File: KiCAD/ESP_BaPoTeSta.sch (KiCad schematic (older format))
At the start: 17 parts, among them P1 Progr, P2 Battery, P3 Power, SW1 Upload, SW2 Reset, U1 MCP1700-3302E, U2 ESP-12, U3 DS18B20

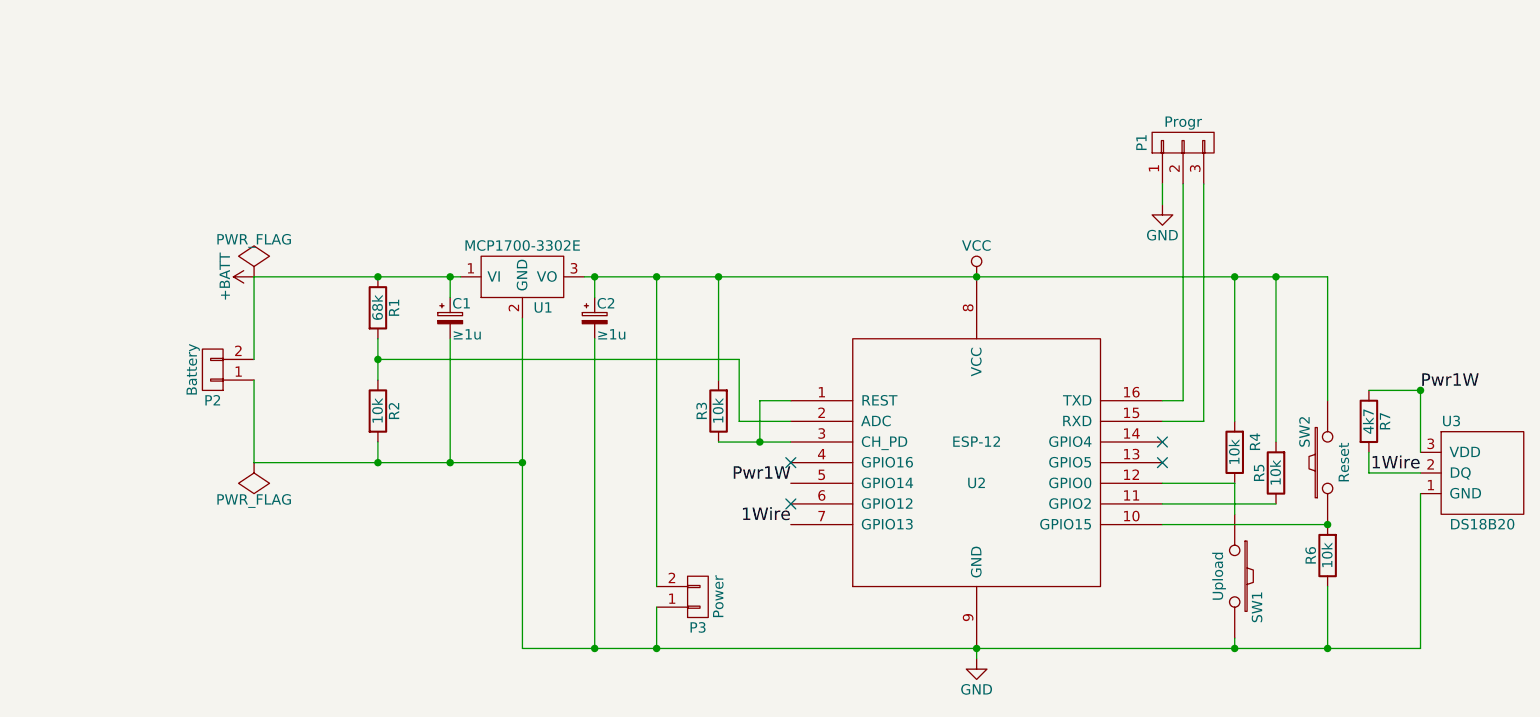
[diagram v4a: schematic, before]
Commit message: WIP: Redesign PCB
Use SMD resistors, and start to work on #14, #15 and #16
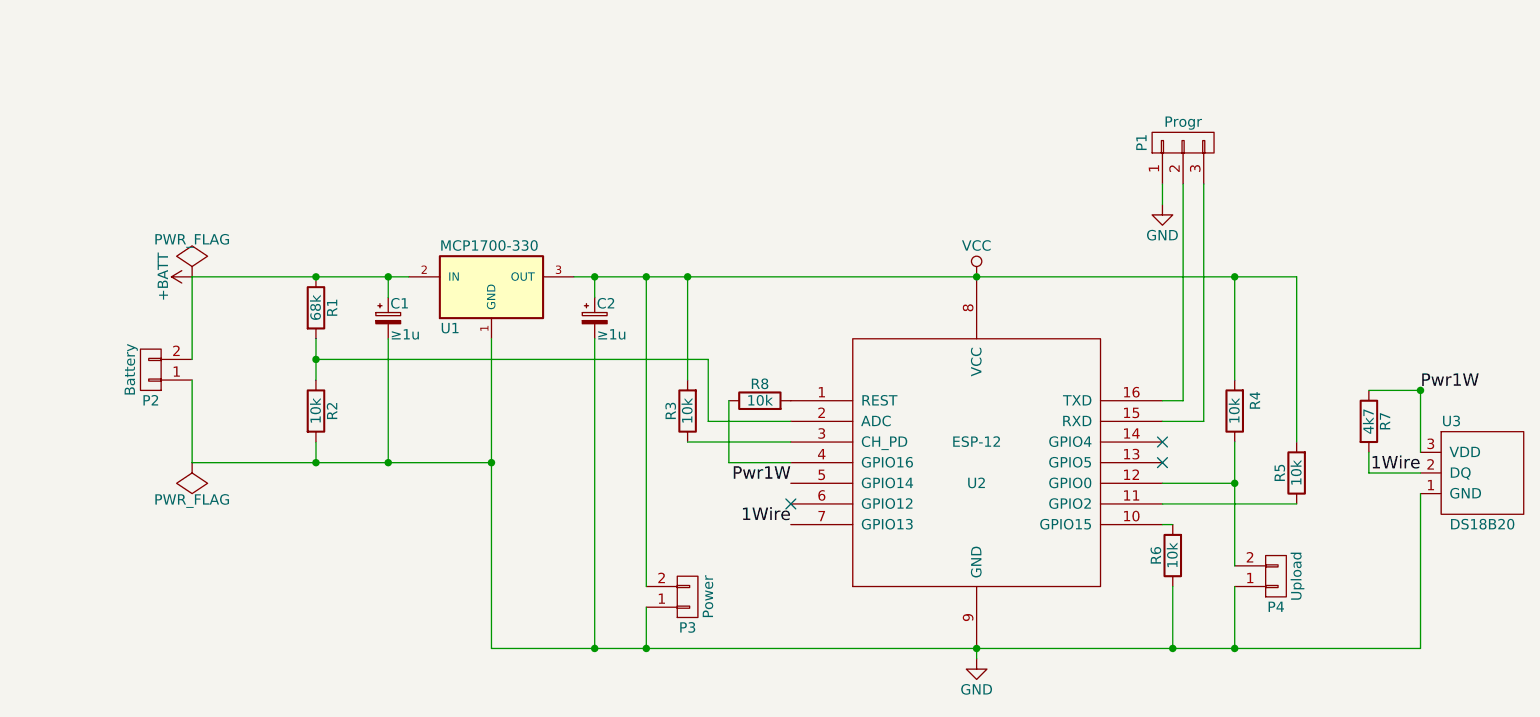
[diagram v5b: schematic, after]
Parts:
- removed SW1: Upload, Buttons_Switches_ThroughHole:SW_PUSH_SMALL, symbol SW_PUSH
- removed SW2: Reset, Buttons_Switches_ThroughHole:SW_PUSH_SMALL, symbol SW_PUSH
- removed U1: MCP1700-3302E, TO_SOT_Packages_THT:TO-92_Inline_Wide, symbol MCP1754ST-3302E/MB
- added P4: Upload, Pin_Headers:Pin_Header_Straight_1x02, symbol CONN_01X02
- added R8: 10k, Resistors_SMD:R_1206_HandSoldering, symbol R
- added U1: MCP1700-330, TO_SOT_Packages_THT:TO-92_Inline_Narrow_Oval, symbol LM7905CT
- R1, R2, R3, R4, R5, R6, R7: footprint Resistors_ThroughHole:Resistor_Horizontal_RM10mm -> Resistors_SMD:R_1206_HandSoldering
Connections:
- net +BATT: now also U1.2 (IN)
- net GND: now also P4.1 (P1), U1.1 (GND)
- net VCC: now also U1.3 (OUT)
- net at R3.1, U2.3 (CH_PD): no longer U2.1 (REST)
- net at R4.1, U2.12 (GPIO0): now also P4.2 (P2)
- net at U2.4 (GPIO16): now also R8.1
- new net: R8.2, U2.1 (REST)
- no-connect marks 4 -> 3
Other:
- moved on the sheet: C1, P2, P3, R1, R2, R3, R4, R5, R6

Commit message: WIP: Continue improving PCB
continue the work started in 0493dcc
add additional header to enter config mode
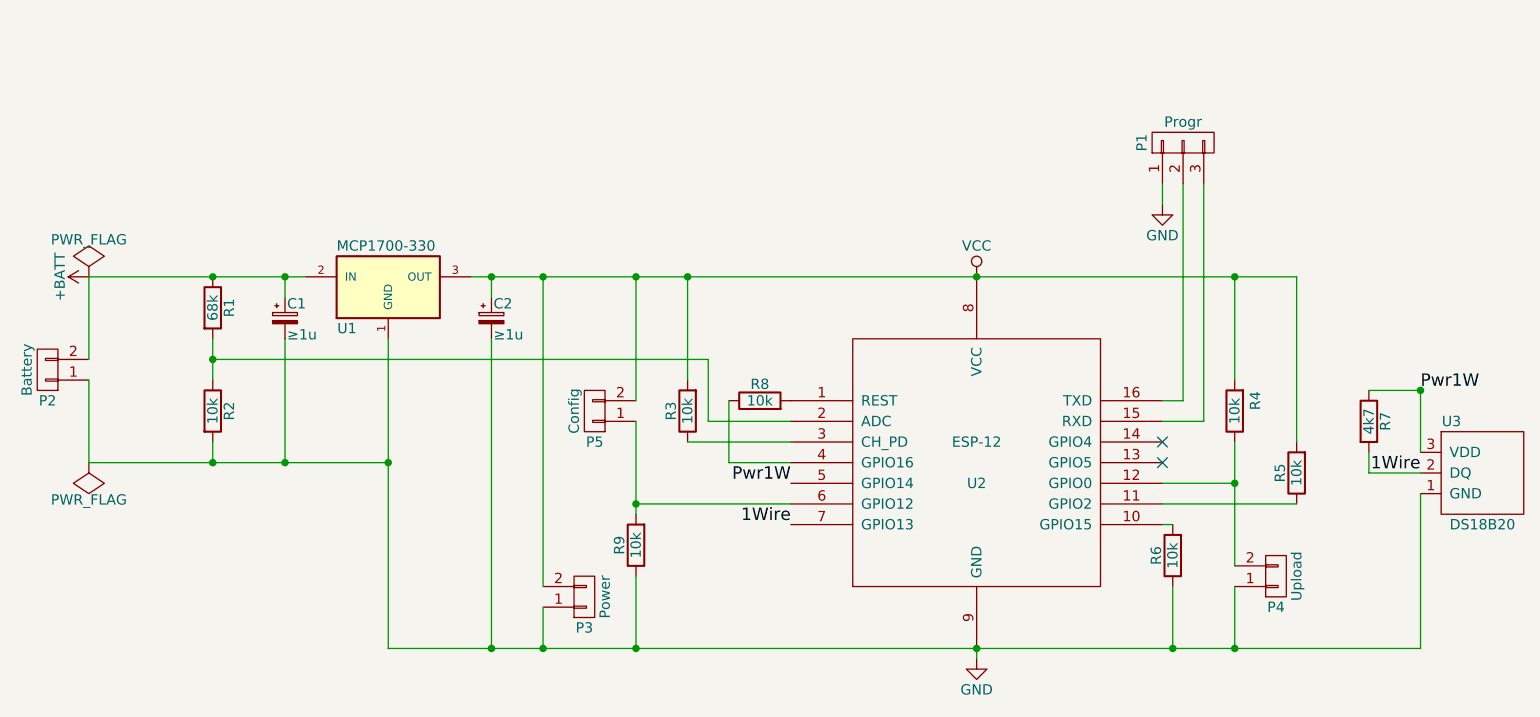
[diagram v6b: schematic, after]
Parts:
- added P5: Config, Pin_Headers:Pin_Header_Straight_1x02, symbol CONN_01X02
- added R9: 10k, Resistors_SMD:R_1206_HandSoldering, symbol R
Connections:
- net GND: now also R9.1
- net VCC: now also P5.2 (P2)
- net at U2.6 (GPIO12): now also P5.1 (P1), R9.2
- no-connect marks 3 -> 2
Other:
- moved on the sheet: C1, C2, P2, P3, R1, R2, U1
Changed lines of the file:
@@
 L R R1
 U 1 1 56629976
-P 2650 2250
-F 0 "R1" V 2730 2250 50  0000 C CNN
-F 1 "68k" V 2650 2250 50  0000 C CNN
-F 2 "Resistors_SMD:R_1206_HandSoldering" V 2580 2250 50  0001 C CNN
-F 3 "" H 2650 2250 50  0000 C CNN
-	1    2650 2250
+P 2150 2250
+F 0 "R1" V 2230 2250 50  0000 C CNN
+F 1 "68k" V 2150 2250 50  0000 C CNN
+F 2 "Resistors_SMD:R_1206_HandSoldering" V 2080 2250 50  0001 C CNN
+F 3 "" H 2150 2250 50  0000 C CNN
+	1    2150 2250
 	1    0    0    -1
 $EndComp
@@
 L R R2
 U 1 1 566299C7
-P 2650 2750
-F 0 "R2" V 2730 2750 50  0000 C CNN
-F 1 "10k" V 2650 2750 50  0000 C CNN
-F 2 "Resistors_SMD:R_1206_HandSoldering" V 2580 2750 50  0001 C CNN
-F 3 "" H 2650 2750 50  0000 C CNN
-	1    2650 2750
+P 2150 2750
+F 0 "R2" V 2230 2750 50  0000 C CNN
+F 1 "10k" V 2150 2750 50  0000 C CNN
+F 2 "Resistors_SMD:R_1206_HandSoldering" V 2080 2750 50  0001 C CNN
+F 3 "" H 2150 2750 50  0000 C CNN
+	1    2150 2750
 	1    0    0    -1
 $EndComp
@@
 Connection ~ 6800 3900
 Wire Wire Line
-	3500 2400 3500 3900
-Wire Wire Line
-	2050 3000 3500 3000
-Wire Wire Line
-	2650 3000 2650 2900
-Wire Wire Line
-	2050 2100 3100 2100
-Wire Wire Line
-	2650 2400 2650 2600
-Connection ~ 2650 2100
-Connection ~ 2650 3000
-Connection ~ 2650 2500
+	3000 2400 3000 3900
+Wire Wire Line
+	1550 3000 3000 3000
+Wire Wire Line
+	2150 3000 2150 2900
+Wire Wire Line
+	1550 2100 2600 2100
+Wire Wire Line
+	2150 2400 2150 2600
+Connection ~ 2150 2100
+Connection ~ 2150 3000
+Connection ~ 2150 2500
 Wire Wire Line
 	4950 2800 4550 2800
@@
 Wire Wire Line
 	8000 3900 8000 3150
-NoConn ~ 4950 3200
 NoConn ~ 6750 2900
 $Comp
@@
 	5850 3900 5850 3950
 Wire Wire Line
-	3500 3900 8000 3900
+	3000 3900 8000 3900
 Connection ~ 4450 2100
 Connection ~ 5850 3900
-Connection ~ 3500 3000
-Wire Wire Line
-	4550 2500 2650 2500
+Connection ~ 3000 3000
+Wire Wire Line
+	4550 2500 2150 2500
 $Comp
 L PWR_FLAG #FLG04
 U 1 1 5662B03F
-P 2050 2100
-F 0 "#FLG04" H 2050 2195 50  0001 C CNN
-F 1 "PWR_FLAG" H 2050 2280 50  0000 C CNN
-F 2 "" H 2050 2100 50  0000 C CNN
-F 3 "" H 2050 2100 50  0000 C CNN
-	1    2050 2100
+P 1550 2100
+F 0 "#FLG04" H 1550 2195 50  0001 C CNN
+F 1 "PWR_FLAG" H 1550 2280 50  0000 C CNN
+F 2 "" H 1550 2100 50  0000 C CNN
+F 3 "" H 1550 2100 50  0000 C CNN
+	1    1550 2100
 	1    0    0    -1
 $EndComp
@@
 L PWR_FLAG #FLG05
 U 1 1 5662B14A
-P 2050 3000
-F 0 "#FLG05" H 2050 3095 50  0001 C CNN
-F 1 "PWR_FLAG" H 2050 3180 50  0000 C CNN
-F 2 "" H 2050 3000 50  0000 C CNN
-F 3 "" H 2050 3000 50  0000 C CNN
-	1    2050 3000
+P 1550 3000
+F 0 "#FLG05" H 1550 3095 50  0001 C CNN
+F 1 "PWR_FLAG" H 1550 3180 50  0000 C CNN
+F 2 "" H 1550 3000 50  0000 C CNN
+F 3 "" H 1550 3000 50  0000 C CNN
+	1    1550 3000
 	-1   0    0    1
 $EndComp
@@
 L CP_Small C1
 U 1 1 5662B5FD
-P 3000 2300
-F 0 "C1" H 3010 2370 50  0000 L CNN
-F 1 "≥1u" H 3010 2220 50  0000 L CNN
-F 2 "Capacitors_ThroughHole:C_Radial_D5_L11_P2" H 3000 2300 50  0001 C CNN
-F 3 "" H 3000 2300 50  0000 C CNN
-	1    3000 2300
+P 2500 2300
+F 0 "C1" H 2510 2370 50  0000 L CNN
+F 1 "≥1u" H 2510 2220 50  0000 L CNN
+F 2 "Capacitors_ThroughHole:C_Radial_D5_L11_P2" H 2500 2300 50  0001 C CNN
+F 3 "" H 2500 2300 50  0000 C CNN
+	1    2500 2300
 	1    0    0    -1
 $EndComp
@@
 L CP_Small C2
 U 1 1 5662B72E
-P 4000 2300
-F 0 "C2" H 4010 2370 50  0000 L CNN
-F 1 "≥1u" H 4010 2220 50  0000 L CNN
-F 2 "Capacitors_ThroughHole:C_Radial_D5_L11_P2" H 4000 2300 50  0001 C CNN
-F 3 "" H 4000 2300 50  0000 C CNN
-	1    4000 2300
-	1    0    0    -1
-$EndComp
-Wire Wire Line
-	4000 2200 4000 2100
-Connection ~ 4000 2100
-Wire Wire Line
-	4000 2400 4000 3900
-Connection ~ 4000 3900
-Wire Wire Line
-	3000 2200 3000 2100
-Connection ~ 3000 2100
-Wire Wire Line
-	3000 2400 3000 3000
-Connection ~ 3000 3000
+P 3500 2300
+F 0 "C2" H 3510 2370 50  0000 L CNN
+F 1 "≥1u" H 3510 2220 50  0000 L CNN
+F 2 "Capacitors_ThroughHole:C_Radial_D5_L11_P2" H 3500 2300 50  0001 C CNN
+F 3 "" H 3500 2300 50  0000 C CNN
+	1    3500 2300
+	1    0    0    -1
+$EndComp
+Wire Wire Line
+	3500 2200 3500 2100
+Connection ~ 3500 2100
+Wire Wire Line
+	3500 2400 3500 3900
+Connection ~ 3500 3900
+Wire Wire Line
+	2500 2200 2500 2100
+Connection ~ 2500 2100
+Wire Wire Line
+	2500 2400 2500 3000
+Connection ~ 2500 3000
 Wire Wire Line
 	7100 2900 7100 3500
@@
 L CONN_01X02 P2
 U 1 1 5662C8D4
-P 1850 2550
-F 0 "P2" H 1850 2700 50  0000 C CNN
-F 1 "Battery" V 1950 2550 50  0000 C CNN
-F 2 "Pin_Headers:Pin_Header_Angled_1x02" H 1850 2550 50  0001 C CNN
-F 3 "" H 1850 2550 50  0000 C CNN
-	1    1850 2550
+P 1350 2550
+F 0 "P2" H 1350 2700 50  0000 C CNN
+F 1 "Battery" V 1450 2550 50  0000 C CNN
+F 2 "Pin_Headers:Pin_Header_Angled_1x02" H 1350 2550 50  0001 C CNN
+F 3 "" H 1350 2550 50  0000 C CNN
+	1    1350 2550
 	-1   0    0    1
 $EndComp
 Wire Wire Line
-	2050 2500 2050 2100
-Wire Wire Line
-	2050 2600 2050 3000
+	1550 2500 1550 2100
+Wire Wire Line
+	1550 2600 1550 3000
 $Comp
 L +BATT #PWR06
 U 1 1 5662D0E0
-P 2050 2100
-F 0 "#PWR06" H 2050 1950 50  0001 C CNN
-F 1 "+BATT" H 2050 2240 50  0000 C CNN
-F 2 "" H 2050 2100 50  0000 C CNN
-F 3 "" H 2050 2100 50  0000 C CNN
-	1    2050 2100
+P 1550 2100
+F 0 "#PWR06" H 1550 1950 50  0001 C CNN
+F 1 "+BATT" H 1550 2240 50  0000 C CNN
+F 2 "" H 1550 2100 50  0000 C CNN
+F 3 "" H 1550 2100 50  0000 C CNN
+	1    1550 2100
 	0    -1   -1   0
 $EndComp
 Wire Wire Line
-	3900 2100 7400 2100
+	3400 2100 7400 2100
 Text Label 4950 3100 2    60   ~ 0
 Pwr1W
@@
 L CONN_01X02 P3
 U 1 1 56659295
-P 4450 3650
-F 0 "P3" H 4450 3800 50  0000 C CNN
-F 1 "Power" V 4550 3650 50  0000 C CNN
-F 2 "Pin_Headers:Pin_Header_Straight_1x02" H 4450 3650 50  0001 C CNN
-F 3 "" H 4450 3650 50  0000 C CNN
-	1    4450 3650
+P 3950 3650
+F 0 "P3" H 3950 3800 50  0000 C CNN
+F 1 "Power" V 4050 3650 50  0000 C CNN
+F 2 "Pin_Headers:Pin_Header_Straight_1x02" H 3950 3650 50  0001 C CNN
+F 3 "" H 3950 3650 50  0000 C CNN
+	1    3950 3650
 	1    0    0    1
 $EndComp
 Wire Wire Line
-	4250 3700 4250 3900
-Connection ~ 4250 3900
-Wire Wire Line
-	4250 3600 4250 2100
-Connection ~ 4250 2100
+	3750 3700 3750 3900
+Connection ~ 3750 3900
+Wire Wire Line
+	3750 3600 3750 2100
+Connection ~ 3750 2100
 $Comp
 L R R8
@@
 L LM7905CT U1
 U 1 1 568D771E
-P 3500 2150
-F 0 "U1" H 3300 2350 50  0000 C CNN
-F 1 "MCP1700-330" H 3250 1950 50  0000 L CNN
-F 2 "TO_SOT_Packages_THT:TO-92_Inline_Narrow_Oval" H 3500 2050 50  0001 C CIN
-F 3 "" H 3500 2150 50  0000 C CNN
-	1    3500 2150
+P 3000 2150
+F 0 "U1" H 2800 2350 50  0000 C CNN
+F 1 "MCP1700-330" H 2750 1950 50  0000 L CNN
+F 2 "TO_SOT_Packages_THT:TO-92_Inline_Narrow_Oval" H 3000 2050 50  0001 C CIN
+F 3 "" H 3000 2150 50  0000 C CNN
+	1    3000 2150
 	1    0    0    1
 $EndComp
@@
 	1    0    0    1
 $EndComp
+$Comp
+L CONN_01X02 P5
+U 1 1 568ED6C5
+P 4000 2750
+F 0 "P5" H 4000 2900 50  0000 C CNN
+F 1 "Config" V 4100 2750 50  0000 C CNN
+F 2 "Pin_Headers:Pin_Header_Straight_1x02" H 4000 2750 50  0001 C CNN
+F 3 "" H 4000 2750 50  0000 C CNN
+	1    4000 2750
+	-1   0    0    1
+$EndComp
+Wire Wire Line
+	4200 2800 4200 3250
+Wire Wire Line
+	4200 3200 4950 3200
+$Comp
+L R R9
+U 1 1 568ED7C9
+P 4200 3400
+F 0 "R9" V 4280 3400 50  0000 C CNN
+F 1 "10k" V 4200 3400 50  0000 C CNN
+F 2 "Resistors_SMD:R_1206_HandSoldering" V 4130 3400 50  0001 C CNN
+F 3 "" H 4200 3400 50  0000 C CNN
+	1    4200 3400
+	-1   0    0    1
+$EndComp
+Connection ~ 4200 3200
+Wire Wire Line
+	4200 3550 4200 3900
+Connection ~ 4200 3900
+Wire Wire Line
+	4200 2700 4200 2100
+Connection ~ 4200 2100
 $EndSCHEMATC

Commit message: ENH: Improve PCB
Finalize work started in 0493dcc and 57554c2
Add DHT22 (you can now install 2 sensors, DHT22 and DS18B20)
Fix the various bugs (fixes #14, fixes #15, fixes #16)
Avoid ground-fill at DS18B20 GND pin (improves accuracy)
Drop the 2 push-buttons
Board now much smaller (3x5cm)
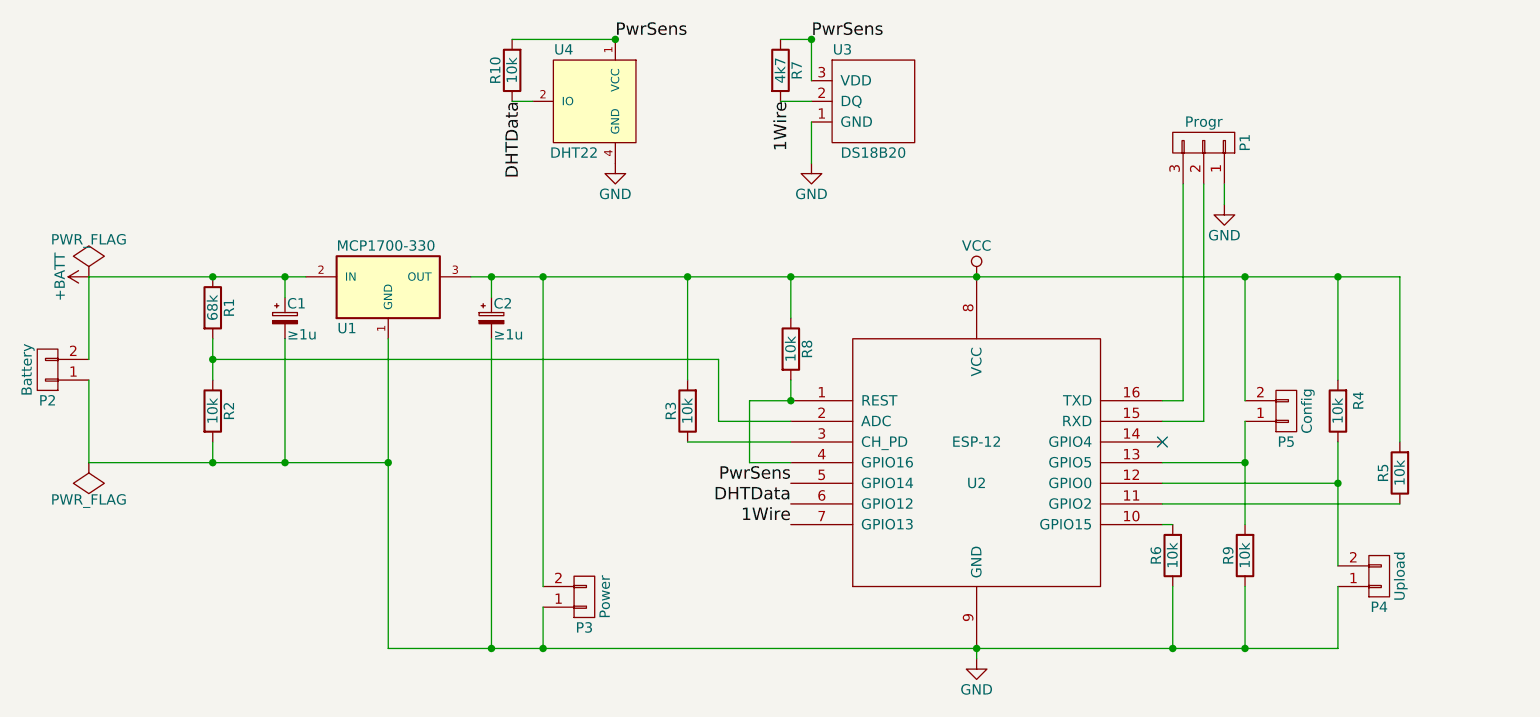
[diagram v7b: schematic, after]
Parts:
- added R10: 10k, Resistors_SMD:R_1206_HandSoldering, symbol R
- added U4: DHT22, Pin_Headers:Pin_Header_Straight_1x04, symbol DHT11
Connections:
- net GND: now also U4.4 (GND)
- net VCC: now also R8.1
- net at R8.2, U2.1 (REST): now also U2.4 (GPIO16)
- net at U2.13 (GPIO5): now also P5.1 (P1), R9.2
- net at U2.15 (RXD): now also P1.2 (P2); no longer P1.3 (P3)
- net at U2.16 (TXD): now also P1.3 (P3); no longer P1.2 (P2)
- net Pwr1W renamed PwrSens
- net PwrSens: now also R10.2, U4.1 (VCC)
- new net DHTData: R10.1, U2.6 (GPIO12), U4.2 (IO)
- no-connect marks 2 -> 1
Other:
- moved on the sheet: P1, P4, P5, R4, R5, R7, R8, R9, U3
